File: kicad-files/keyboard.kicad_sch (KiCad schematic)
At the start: 164 parts, among them J1 TYPE-C-31-M12_13, U1 STM32F411CEU6, U2 USBLC6-2SC6, U3 AT24C256C-SSHL-T, U4 SGM2007-3.3XN5/TR, Y1 TAXM8M4RFDCET2T

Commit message: Rename row and col to use captial
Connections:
- net c0 renamed C0
- net c1 renamed C1
- net c10 renamed C10
- net c11 renamed C11
- net c12 renamed C12
- net c13 renamed C13
- net c14 renamed C14
- net c15 renamed C15
- net c16 renamed C16
- net c2 renamed C2
- net c3 renamed C3
- net c4 renamed C4
- net c5 renamed C5
- net c6 renamed C6
- net c7 renamed C7
- net c8 renamed C8
- net c9 renamed C9
- net r0 renamed R0
- net r1 renamed R1
- net r2 renamed R2
- net r3 renamed R3
- net r4 renamed R4
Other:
- moved on the sheet: FB1
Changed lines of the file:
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@@
     (stroke (width 0) (type default))
   )
-  (wire (pts (xy 57.15 241.3) (xy 57.15 243.84))
+  (wire (pts (xy 54.61 248.92) (xy 54.61 251.46))
     (stroke (width 0) (type default))
   )
@@
     (stroke (width 0) (type default))
   )
-  (wire (pts (xy 57.15 231.14) (xy 57.15 233.68))
+  (wire (pts (xy 54.61 238.76) (xy 54.61 241.3))
     (stroke (width 0) (type default))
   )
@@
     )
   )
-  (global_label "r3" (shape input) (at 22.86 111.76 180)
+  (global_label "R3" (shape input) (at 22.86 111.76 180)
     (effects (font (size 1.27 1.27)) (justify right))
     (property "Intersheetrefs" "${INTERSHEET_REFS}" (at 22.86 111.76 0)
@@
     )
   )
-  (global_label "c9" (shape input) (at 274.32 16.51 180)
+  (global_label "C9" (shape input) (at 274.32 16.51 180)
     (effects (font (size 1.27 1.27)) (justify right))
     (property "Intersheetrefs" "${INTERSHEET_REFS}" (at 274.32 16.51 0)
@@
     )
   )
-  (global_label "c3" (shape input) (at 121.92 16.51 180)
+  (global_label "C3" (shape input) (at 121.92 16.51 180)
     (effects (font (size 1.27 1.27)) (justify right))
     (property "Intersheetrefs" "${INTERSHEET_REFS}" (at 121.92 16.51 0)
@@
     )
   )
-  (global_label "c1" (shape input) (at 71.12 16.51 180)
+  (global_label "C1" (shape input) (at 71.12 16.51 180)
     (effects (font (size 1.27 1.27)) (justify right))
     (property "Intersheetrefs" "${INTERSHEET_REFS}" (at 71.12 16.51 0)
@@
     )
   )
-  (global_label "c4" (shape input) (at 147.32 16.51 180)
+  (global_label "C4" (shape input) (at 147.32 16.51 180)
     (effects (font (size 1.27 1.27)) (justify right))
     (property "Intersheetrefs" "${INTERSHEET_REFS}" (at 147.32 16.51 0)
@@
     )
   )
-  (global_label "c6" (shape input) (at 198.12 16.51 180)
+  (global_label "C6" (shape input) (at 198.12 16.51 180)
     (effects (font (size 1.27 1.27)) (justify right))
     (property "Intersheetrefs" "${INTERSHEET_REFS}" (at 198.12 16.51 0)
@@
     )
   )
-  (global_label "c15" (shape input) (at 426.72 16.51 180)
+  (global_label "C15" (shape input) (at 426.72 16.51 180)
     (effects (font (size 1.27 1.27)) (justify right))
     (property "Intersheetrefs" "${INTERSHEET_REFS}" (at 426.72 16.51 0)
@@
     )
   )
-  (global_label "c13" (shape input) (at 375.92 16.51 180)
+  (global_label "C13" (shape input) (at 375.92 16.51 180)
     (effects (font (size 1.27 1.27)) (justify right))
     (property "Intersheetrefs" "${INTERSHEET_REFS}" (at 375.92 16.51 0)
@@
     )
   )
-  (global_label "r2" (shape input) (at 22.86 86.36 180)
+  (global_label "R2" (shape input) (at 22.86 86.36 180)
     (effects (font (size 1.27 1.27)) (justify right))
     (property "Intersheetrefs" "${INTERSHEET_REFS}" (at 22.86 86.36 0)
@@
     )
   )
-  (global_label "c7" (shape input) (at 223.52 16.51 180)
+  (global_label "C7" (shape input) (at 223.52 16.51 180)
     (effects (font (size 1.27 1.27)) (justify right))
     (property "Intersheetrefs" "${INTERSHEET_REFS}" (at 223.52 16.51 0)
@@
     )
   )
-  (global_label "c2" (shape input) (at 96.52 16.51 180)
+  (global_label "C2" (shape input) (at 96.52 16.51 180)
     (effects (font (size 1.27 1.27)) (justify right))
     (property "Intersheetrefs" "${INTERSHEET_REFS}" (at 96.52 16.51 0)
@@
     )
   )
-  (global_label "r0" (shape input) (at 22.86 35.56 180)
+  (global_label "R0" (shape input) (at 22.86 35.56 180)
     (effects (font (size 1.27 1.27)) (justify right))
     (property "Intersheetrefs" "${INTERSHEET_REFS}" (at 22.86 35.56 0)
@@
     )
   )
-  (global_label "c5" (shape input) (at 172.72 16.51 180)
+  (global_label "C5" (shape input) (at 172.72 16.51 180)
     (effects (font (size 1.27 1.27)) (justify right))
     (property "Intersheetrefs" "${INTERSHEET_REFS}" (at 172.72 16.51 0)
@@
     )
   )
-  (global_label "c16" (shape input) (at 452.12 16.51 180)
+  (global_label "C16" (shape input) (at 452.12 16.51 180)
     (effects (font (size 1.27 1.27)) (justify right))
     (property "Intersheetrefs" "${INTERSHEET_REFS}" (at 452.12 16.51 0)
@@
     )
   )
-  (global_label "c8" (shape input) (at 248.92 16.51 180)
+  (global_label "C8" (shape input) (at 248.92 16.51 180)
     (effects (font (size 1.27 1.27)) (justify right))
     (property "Intersheetrefs" "${INTERSHEET_REFS}" (at 248.92 16.51 0)
@@
     )
   )
-  (global_label "r1" (shape input) (at 22.86 60.96 180)
+  (global_label "R1" (shape input) (at 22.86 60.96 180)
     (effects (font (size 1.27 1.27)) (justify right))
     (property "Intersheetrefs" "${INTERSHEET_REFS}" (at 22.86 60.96 0)
@@
     )
   )
-  (global_label "c10" (shape input) (at 299.72 16.51 180)
+  (global_label "C10" (shape input) (at 299.72 16.51 180)
     (effects (font (size 1.27 1.27)) (justify right))
     (property "Intersheetrefs" "${INTERSHEET_REFS}" (at 299.72 16.51 0)
@@
     )
   )
-  (global_label "r4" (shape input) (at 22.86 137.16 180)
+  (global_label "R4" (shape input) (at 22.86 137.16 180)
     (effects (font (size 1.27 1.27)) (justify right))
     (property "Intersheetrefs" "${INTERSHEET_REFS}" (at 22.86 137.16 0)
@@
     )
   )
-  (global_label "c11" (shape input) (at 325.12 16.51 180)
+  (global_label "C11" (shape input) (at 325.12 16.51 180)
     (effects (font (size 1.27 1.27)) (justify right))
     (property "Intersheetrefs" "${INTERSHEET_REFS}" (at 325.12 16.51 0)
@@
     )
   )
-  (global_label "c12" (shape input) (at 350.52 16.51 180)
+  (global_label "C12" (shape input) (at 350.52 16.51 180)
     (effects (font (size 1.27 1.27)) (justify right))
     (property "Intersheetrefs" "${INTERSHEET_REFS}" (at 350.52 16.51 0)
@@
     )
   )
-  (global_label "c14" (shape input) (at 401.32 16.51 180)
+  (global_label "C14" (shape input) (at 401.32 16.51 180)
     (effects (font (size 1.27 1.27)) (justify right))
     (property "Intersheetrefs" "${INTERSHEET_REFS}" (at 401.32 16.51 0)
@@
     )
   )
-  (global_label "c0" (shape input) (at 45.72 16.51 180)
+  (global_label "C0" (shape input) (at 45.72 16.51 180)
     (effects (font (size 1.27 1.27)) (justify right))
     (property "Intersheetrefs" "${INTERSHEET_REFS}" (at 45.72 16.51 0)
@@
     )
   )
-  (symbol (lib_id "power:GNDPWR") (at 57.15 231.14 180) (unit 1)
+  (symbol (lib_id "power:GNDPWR") (at 54.61 238.76 180) (unit 1)
     (in_bom yes) (on_board yes) (dnp no) (fields_autoplaced)
-    (property "Reference" "#PWR06" (at 57.15 226.06 0)
+    (property "Reference" "#PWR06" (at 54.61 233.68 0)
       (effects (font (size 1.27 1.27)) hide)
     )
-    (property "Value" "GNDPWR" (at 57.277 227.33 0)
+    (property "Value" "GNDPWR" (at 54.737 234.95 0)
       (effects (font (size 1.27 1.27)))
     )
-    (property "Footprint" "" (at 57.15 229.87 0)
+    (property "Footprint" "" (at 54.61 237.49 0)
       (effects (font (size 1.27 1.27)) hide)
     )
-    (property "Datasheet" "" (at 57.15 229.87 0)
+    (property "Datasheet" "" (at 54.61 237.49 0)
       (effects (font (size 1.27 1.27)) hide)
     )
@@
     )
   )
-  (symbol (lib_id "Device:FerriteBead") (at 57.15 237.49 0) (unit 1)
+  (symbol (lib_id "Device:FerriteBead") (at 54.61 245.11 0) (unit 1)
     (in_bom yes) (on_board yes) (dnp no)
-    (property "Reference" "FB1" (at 49.53 238.76 0)
+    (property "Reference" "FB1" (at 46.99 246.38 0)
       (effects (font (size 1.27 1.27)) (justify left))
     )
-    (property "Value" "GZ2012D601TF" (at 49.53 241.3 0)
+    (property "Value" "GZ2012D601TF" (at 46.99 248.92 0)
       (effects (font (size 1.27 1.27)) (justify left))
     )
-    (property "Footprint" "Inductor_SMD:L_0805_2012Metric_Pad1.05x1.20mm_HandSolder" (at 55.372 237.49 90)
+    (property "Footprint" "Inductor_SMD:L_0805_2012Metric_Pad1.05x1.20mm_HandSolder" (at 52.832 245.11 90)
       (effects (font (size 1.27 1.27)) hide)
     )
-    (property "Datasheet" "~" (at 57.15 237.49 0)
+    (property "Datasheet" "~" (at 54.61 245.11 0)
       (effects (font (size 1.27 1.27)) hide)
     )
@@
     )
   )
-  (symbol (lib_id "power:GND") (at 57.15 243.84 0) (unit 1)
+  (symbol (lib_id "power:GND") (at 54.61 251.46 0) (unit 1)
     (in_bom yes) (on_board yes) (dnp no)
-    (property "Reference" "#PWR05" (at 57.15 250.19 0)
+    (property "Reference" "#PWR05" (at 54.61 257.81 0)
       (effects (font (size 1.27 1.27)) hide)
     )
-    (property "Value" "GND" (at 57.15 247.65 0)
+    (property "Value" "GND" (at 54.61 255.27 0)
       (effects (font (size 1.27 1.27)))
     )
-    (property "Footprint" "" (at 57.15 243.84 0)
+    (property "Footprint" "" (at 54.61 251.46 0)
       (effects (font (size 1.27 1.27)) hide)
     )
-    (property "Datasheet" "" (at 57.15 243.84 0)
+    (property "Datasheet" "" (at 54.61 251.46 0)
       (effects (font (size 1.27 1.27)) hide)
     )

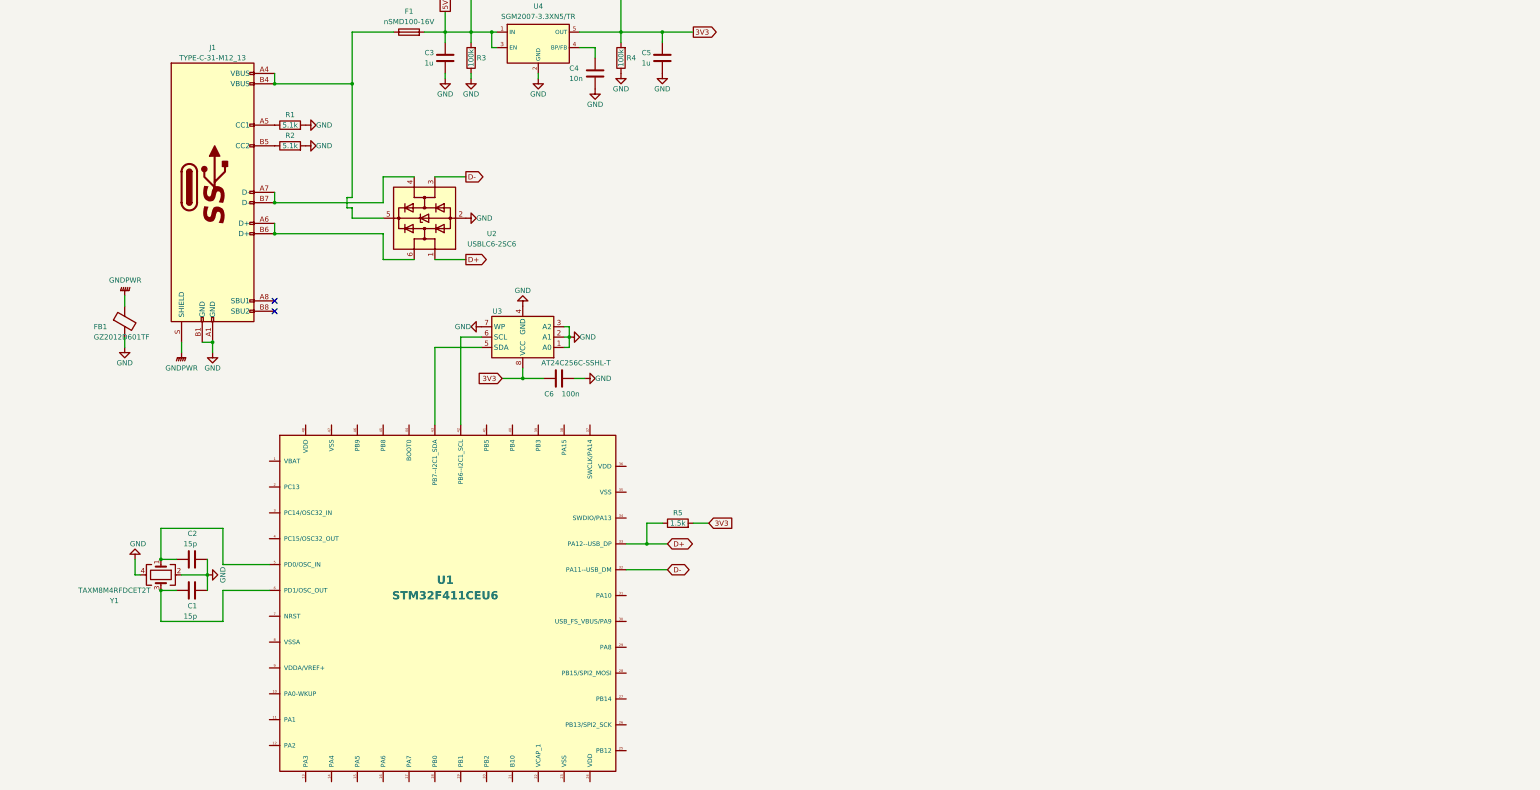
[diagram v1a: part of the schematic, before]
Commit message: Added reset switch
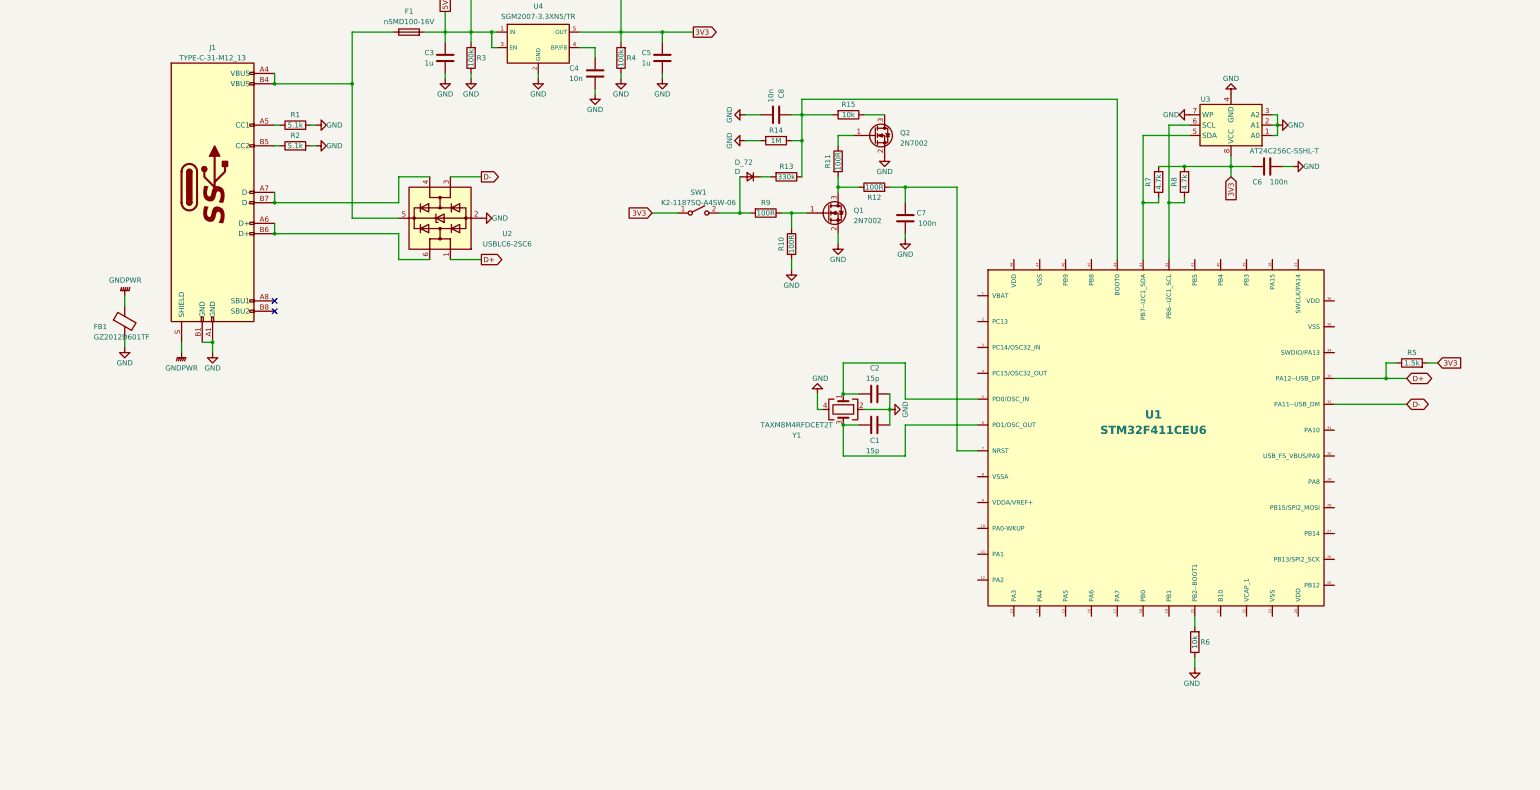
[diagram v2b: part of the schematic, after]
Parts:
- added C7: 100n, Capacitor_SMD:C_0603_1608Metric_Pad1.08x0.95mm_HandSolder, symbol Device:C
- added C8: 10n, Capacitor_SMD:C_0603_1608Metric_Pad1.08x0.95mm_HandSolder, symbol Device:C
- added D_72: D, Diode_SMD:D_SOD-123, symbol Device:D_Small
- added Q1, Q2: 2N7002, Package_TO_SOT_SMD:SOT-23, symbol Transistor_FET:2N7002
- added R10, R11, R12, R9: 100R, Resistor_SMD:R_0603_1608Metric, symbol Device:R
- added R13: 330k, Resistor_SMD:R_0603_1608Metric, symbol Device:R
- added R14: 1M, Resistor_SMD:R_0603_1608Metric, symbol Device:R
- added R15, R6: 10k, Resistor_SMD:R_0603_1608Metric, symbol Device:R
- added R7, R8: 4.7k, Resistor_SMD:R_0603_1608Metric, symbol Device:R
- added SW1: K2-1187SQ-A4SW-06, acheron_Hardware:K2-1187SQ-A4SW-06, symbol Switch:SW_SPST
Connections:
- net 3V3: now also R7.2, R8.2, SW1.1 (A)
- net GND: now also C7.1, C8.2, Q1.2 (S), Q2.2 (S), R10.2, R14.2, R6.1
- net at U1.43 (PB7--I2C1_SDA), U3.5 (SDA): now also R7.1
- net at U1.42 (PB6--I2C1_SCL), U3.6 (SCL): now also R8.1
- net at U1.20 (PB2--BOOT1): now also R6.2
- net at U1.44 (BOOT0): now also C8.1, R13.1, R14.1, R15.2
- net at U1.7 (NRST): now also C7.2, R12.2
- new net: Q1.3 (D), R11.2, R12.1
- new net: Q2.1 (G), R11.1
- new net: D_72.1 (K), R13.2
- new net: Q1.1 (G), R10.1, R9.1
- new net: D_72.2 (A), R9.2, SW1.2 (B)
- new net: Q2.3 (D), R15.1
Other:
- moved on the sheet: C1, C2, C6, R1, R2, R5, U1, U2, U3, Y1
